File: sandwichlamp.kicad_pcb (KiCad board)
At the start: 2 copper layers, 96 x 96 mm, 7 parts, among them J1 Conn_01x01_Pin, J2 Conn_01x01_Pin, J3 Conn_01x01_Pin, U1 magnetic-charger, U2 esp32-wemos-d1-mini, U3 hw357

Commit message: Update PCB
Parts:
- added J4: 12V Enable, Connector_PinHeader_2.54mm:PinHeader_1x01_P2.54mm_Vertical, F.Cu at (79.9, 91.0)
- added SW1: SW_SPDT, Connector_PinHeader_2.54mm:PinHeader_1x03_P2.54mm_Vertical, F.Cu at (81.3, 100.1)
- moved J2 0.22 mm to (136.5, 120.8), turned to -120 degrees
- moved J1 0.20 mm to (100.0, 58.0)
- moved J3 0.16 mm to (63.6, 120.9), turned to 120 degrees
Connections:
- U2 pad 1: unconnected-(U2-GND-Pad1) -> GND
- U2 pad 16: unconnected-(U2-3V3-Pad16) -> +3V3
- U2 pad 22: unconnected-(U2-GND-Pad22) -> GND
- U2 pad 33: unconnected-(U2-GND-Pad33) -> GND
- U2 pad 35: unconnected-(U2-VCC_(USB)-Pad35) -> +5V
- U3 pad 2: unconnected-(U3-IN--Pad2) -> GND
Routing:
- added copper zone on B.Cu, net GND

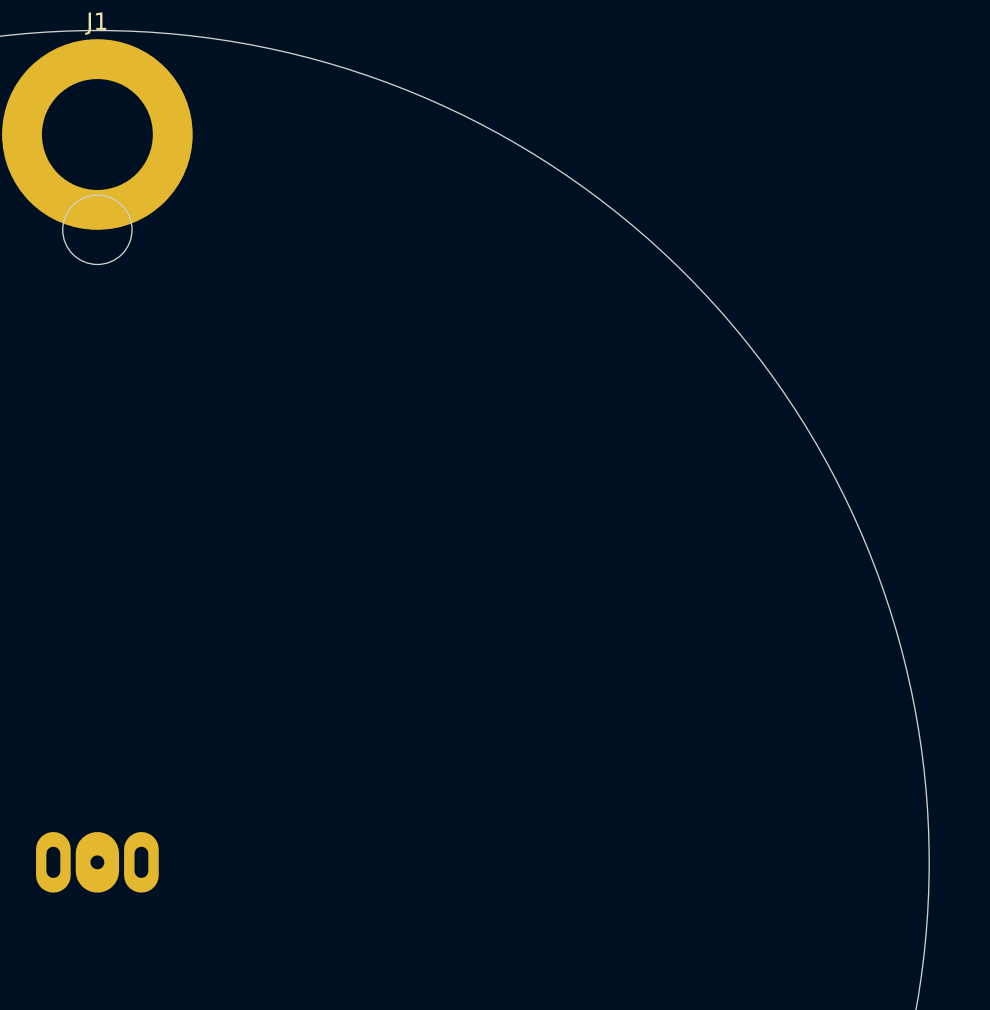
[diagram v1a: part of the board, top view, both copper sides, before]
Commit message: Add radar sensor
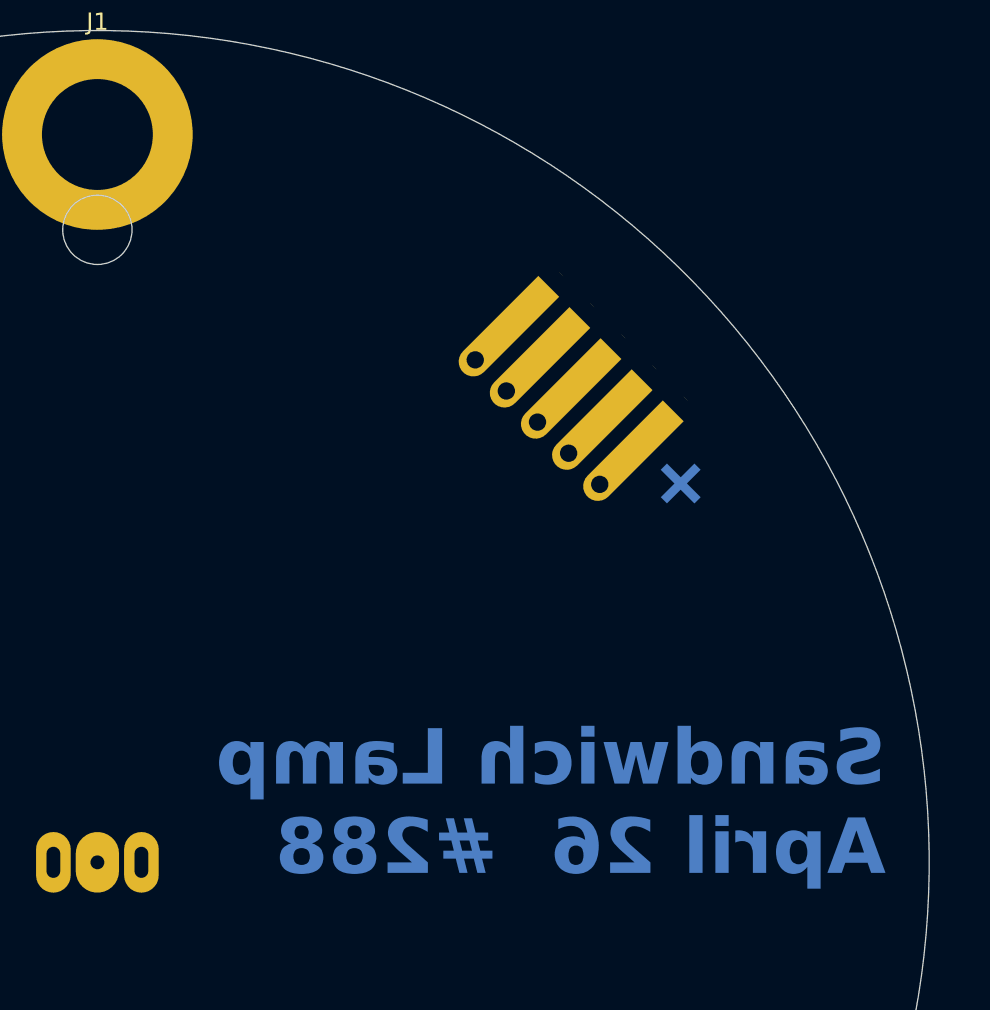
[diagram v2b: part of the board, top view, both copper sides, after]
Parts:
- added J8: HLK-LD2410C, Connector_PinHeader_2.54mm:PinHeader_1x05_P2.54mm_Vertical, B.Cu at (129.0, 78.2)
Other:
- board text added: "Sandwich Lamp April 26 #288"

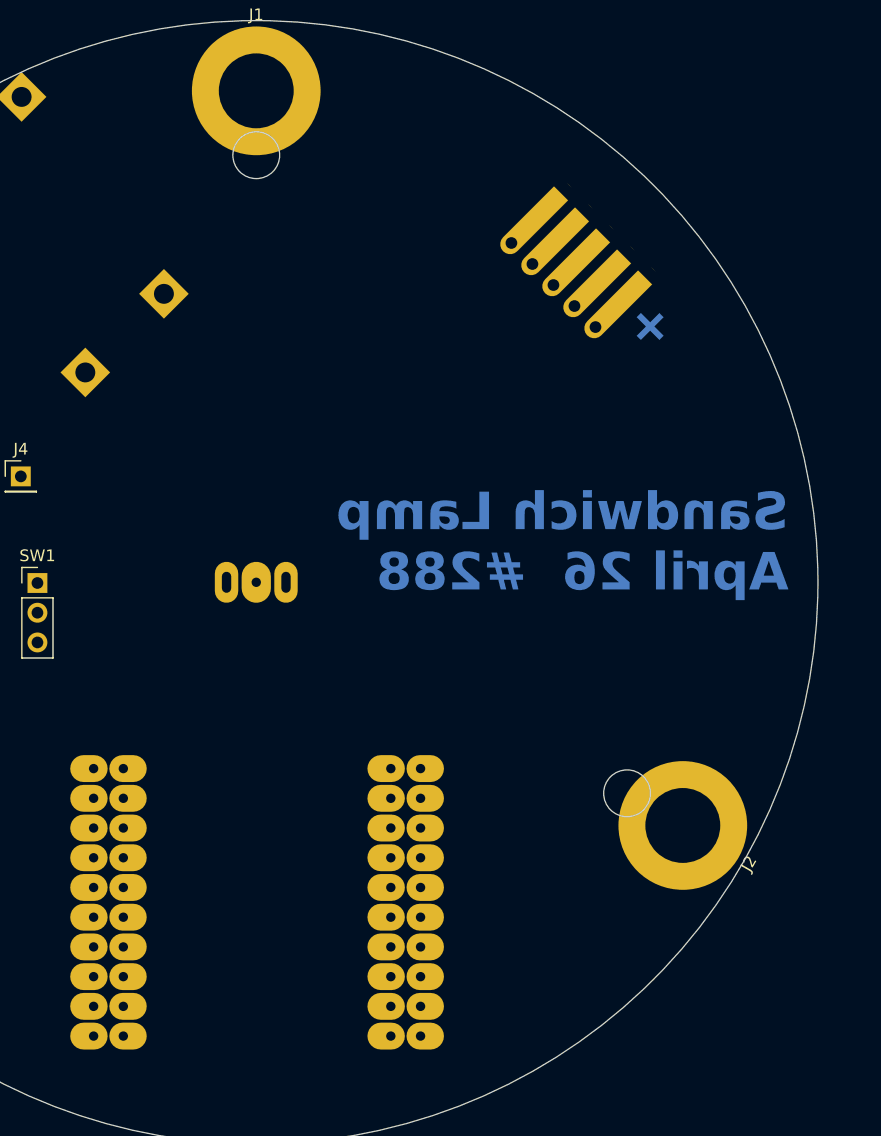
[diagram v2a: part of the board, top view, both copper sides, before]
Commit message: Align the radar with the cable
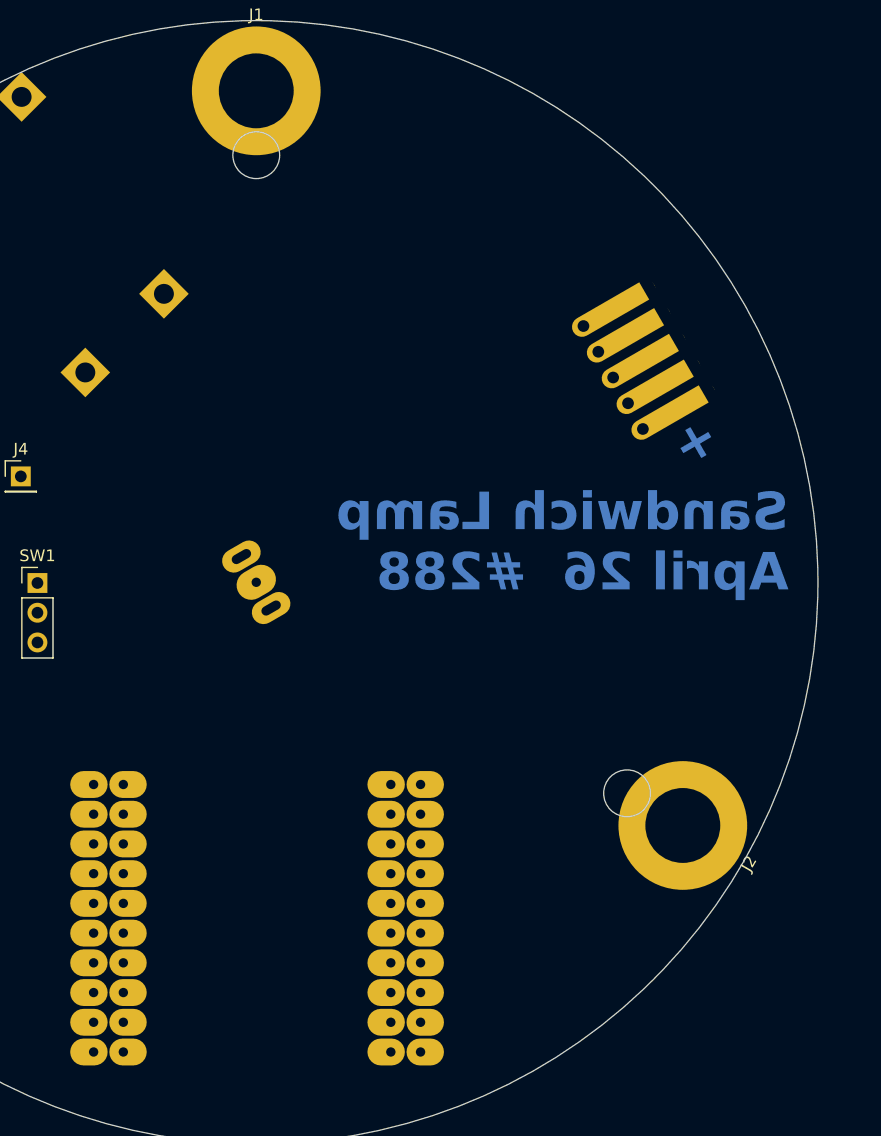
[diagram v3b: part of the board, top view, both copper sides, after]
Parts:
- moved J8 9.61 mm to (133.0, 86.9), turned to 30 degrees
- moved U2 1.36 mm to (100.1, 128.7)
- turned U1 to 120 degrees
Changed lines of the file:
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@@
 	(footprint "Connector_PinHeader_2.54mm:PinHeader_1x05_P2.54mm_Vertical"
 		(layer "B.Cu")
-		(at 128.988567 78.188567 45)
+		(at 133.04 86.899409 30)
 		(descr "Through hole straight pin header, 1x05, 2.54mm pitch, single row")
 		(tags "Through hole pin header THT 1x05 2.54mm single row")
 		(property "Reference" "J8"
-			(at 0 2.33 -135)
+			(at 0 2.33 30)
 			(layer "B.SilkS")
 			(effects
@@
 		)
 		(property "Value" "HLK-LD2410C"
-			(at 0 -12.49 -135)
+			(at 0 -12.490001 30)
 			(layer "B.Fab")
 			(effects
@@
 		)
 		(property "Footprint" ""
-			(at 0 0 -135)
+			(at 0 0 30)
 			(layer "F.Fab")
 			(hide yes)
@@
 		)
 		(property "Datasheet" ""
-			(at 0 0 -135)
+			(at 0 0 30)
 			(layer "F.Fab")
 			(hide yes)
@@
 		)
 		(property "Description" "Generic connector, single row, 01x05, script generated (kicad-library-utils/schlib/autogen/connector/)"
-			(at 0 0 -135)
+			(at 0 0 30)
 			(layer "F.Fab")
 			(hide yes)
@@
 		)
 		(property "Price" "4"
-			(at 189.916309 -70.530043 -45)
+			(at 189.91631 -70.530043 120)
 			(layer "B.Fab")
 			(hide yes)
@@
 		)
 		(property "URL" "https://de.aliexpress.com/item/1005005400130647.html"
-			(at 189.916309 -70.530043 -45)
+			(at 189.91631 -70.530043 120)
 			(layer "B.Fab")
 			(hide yes)
@@
 		)
 		(fp_line
-			(start -1.8 -11.95)
-			(end 1.8 -11.95)
+			(start -1.799999 -11.95)
+			(end 1.799999 -11.95)
 			(stroke
 				(width 0.05)
@@
 		)
 		(fp_line
-			(start 1.8 -11.95)
-			(end 1.8 1.8)
+			(start 1.799999 -11.95)
+			(end 1.799999 1.8)
 			(stroke
 				(width 0.05)
@@
 		)
 		(fp_line
-			(start -1.8 1.8)
-			(end -1.8 -11.95)
+			(start -1.8 1.799999)
+			(end -1.799999 -11.95)
 			(stroke
 				(width 0.05)
@@
 		)
 		(fp_line
-			(start 1.8 1.8)
-			(end -1.8 1.8)
+			(start 1.799999 1.8)
+			(end -1.8 1.799999)
 			(stroke
 				(width 0.05)
@@
 		)
 		(fp_text user "+"
-			(at 1.5 1.5 -135)
+			(at 1.5 1.5 -150)
 			(unlocked yes)
 			(layer "B.Cu" knockout)
@@
 		)
 		(fp_text user "${REFERENCE}"
-			(at 0 -5.079999 -45)
+			(at 0 -5.08 120)
 			(layer "B.Fab")
 			(effects
@@
 		)
 		(pad "" np_thru_hole circle
-			(at 6.5 -5 45)
+			(at 6.5 -5 30)
 			(size 0.8 0.8)
 			(drill oval 1 22)
@@
 		)
 		(pad "" np_thru_hole circle
-			(at 8.25 8.500001 90)
+			(at 8.25 8.5 75)
 			(size 0.8 0.8)
 			(drill oval 1 6)
@@
 		)
 		(pad "" np_thru_hole circle
-			(at 8.4 -18.4)
+			(at 8.4 -18.400001 345)
 			(size 0.8 0.8)
 			(drill oval 1 6)
@@
 		)
 		(pad "1" thru_hole oval
-			(at 0 0 45)
+			(at 0 0 30)
 			(size 8 1.7)
 			(drill 1
@@
 		)
 		(pad "2" thru_hole oval
-			(at 0 -2.54 45)
+			(at 0 -2.54 30)
 			(size 8 1.7)
 			(drill 1
@@
 		)
 		(pad "3" thru_hole oval
-			(at 0 -5.079999 45)
+			(at 0 -5.08 30)
 			(size 8 1.7)
 			(drill 1
@@
 		)
 		(pad "4" thru_hole oval
-			(at 0 -7.62 45)
+			(at 0 -7.62 30)
 			(size 8 1.7)
 			(drill 1
@@
 		)
 		(pad "5" thru_hole oval
-			(at 0 -10.16 45)
+			(at 0 -10.16 30)
 			(size 8 1.7)
 			(drill 1
@@
 	(footprint "magnetic-charger:magnetic-charger"
 		(layer "B.Cu")
-		(at 100 100 180)
+		(at 100 100 120)
 		(property "Reference" "U1"
-			(at 0 2.54 0)
+			(at 0 2.54 -60)
 			(unlocked yes)
 			(layer "B.SilkS")
@@
 		)
 		(property "Value" "magnetic-charger"
-			(at 10.16 14.2 0)
+			(at 10.16 14.2 -60)
 			(unlocked yes)
 			(layer "B.Fab")
@@
 		)
 		(property "Footprint" "magnetic-charger:magnetic-charger"
-			(at 0 0 0)
+			(at 0 0 120)
 			(layer "B.Fab")
 			(hide yes)
@@
 		)
 		(property "Datasheet" ""
-			(at 0 0 0)
+			(at 0 0 120)
 			(layer "B.Fab")
 			(hide yes)
@@
 		)
 		(property "Description" ""
-			(at 0 0 0)
+			(at 0 0 120)
 			(layer "B.Fab")
 			(hide yes)
@@
 		(sheetfile "sandwichlamp.kicad_sch")
 		(attr through_hole)
+		(fp_line
+			(start 0.5 -14)
+			(end 0.5 -8)
+			(stroke
+				(width 0.1)
+				(type dot)
+			)
+			(layer "B.SilkS")
+		)
+		(fp_line
+			(start -0.5 -13.5)
+			(end 0.5 -14)
+			(stroke
+				(width 0.1)
+				(type dot)
+			)
+			(layer "B.SilkS")
+		)
+		(fp_line
+			(start 1.5 -8)
+			(end 1.5 -6)
+			(stroke
+				(width 0.1)
+				(type dot)
+			)
+			(layer "B.SilkS")
+		)
+		(fp_line
+			(start -0.5 -8)
+			(end -0.5 -13.5)
+			(stroke
+				(width 0.1)
+				(type dot)
+			)
+			(layer "B.SilkS")
+		)
+		(fp_line
+			(start -1.5 -8)
+			(end 1.5 -8)
+			(stroke
+				(width 0.1)
+				(type dot)
+			)
+			(layer "B.SilkS")
+		)
+		(fp_line
+			(start -1.5 -6)
+			(end -1.5 -8)
+			(stroke
+				(width 0.1)
+				(type dot)
+			)
+			(layer "B.SilkS")
+		)
 		(fp_circle
 			(center 0 0)
@@
 			(stroke
 				(width 0.12)
-				(type solid)
+				(type dot)
 			)
 			(fill none)
@@
 		)
 		(fp_text user "${REFERENCE}"
-			(at 10.16 12.7 0)
+			(at 10.16 12.7 -60)
 			(unlocked yes)
 			(layer "B.Fab")
@@
 		)
 		(pad "1" thru_hole oval
-			(at -2.54 0 90)
+			(at -2.54 0 30)
 			(size 3.5 2)
 			(drill oval 1.8 0.8)
@@
 		)
 		(pad "1" thru_hole oval
-			(at 2.54 0 90)
+			(at 2.54 0 30)
 			(size 3.5 2)
 			(drill oval 1.8 0.8)
@@
 		)
 		(pad "2" thru_hole oval
-			(at 0 0 180)
+			(at 0 0 120)
 			(size 2.5 3.5)
 			(drill 0.8)
@@
 	(footprint "esp32-wemos-d1-mini:esp32-wemos-d1-mini"
 		(layer "B.Cu")
-		(at 100.07 127.35 180)
+		(at 100.07 128.71 180)
 		(property "Reference" "U2"
 			(at -3.81 -1.27 0)
@@
 			)
 		)
+	)
+	(gr_line
+		(start 100 100)
+		(end 141.568668 76.000319)
+		(stroke
+			(width 0.1)
+			(type default)
+		)
+		(layer "Dwgs.User")
 	)
 	(gr_circle
@@
 	(gr_line
 		(start 100 100)
-		(end 148.26 51.74)
+		(end 141.568668 123.999681)
 		(stroke
 			(width 0.1)
+			(type default)
+		)
+		(layer "Dwgs.User")
+	)
+	(gr_line
+		(start 100 100)
+		(end 58.430781 124)
+		(stroke
+			(width 0.1)

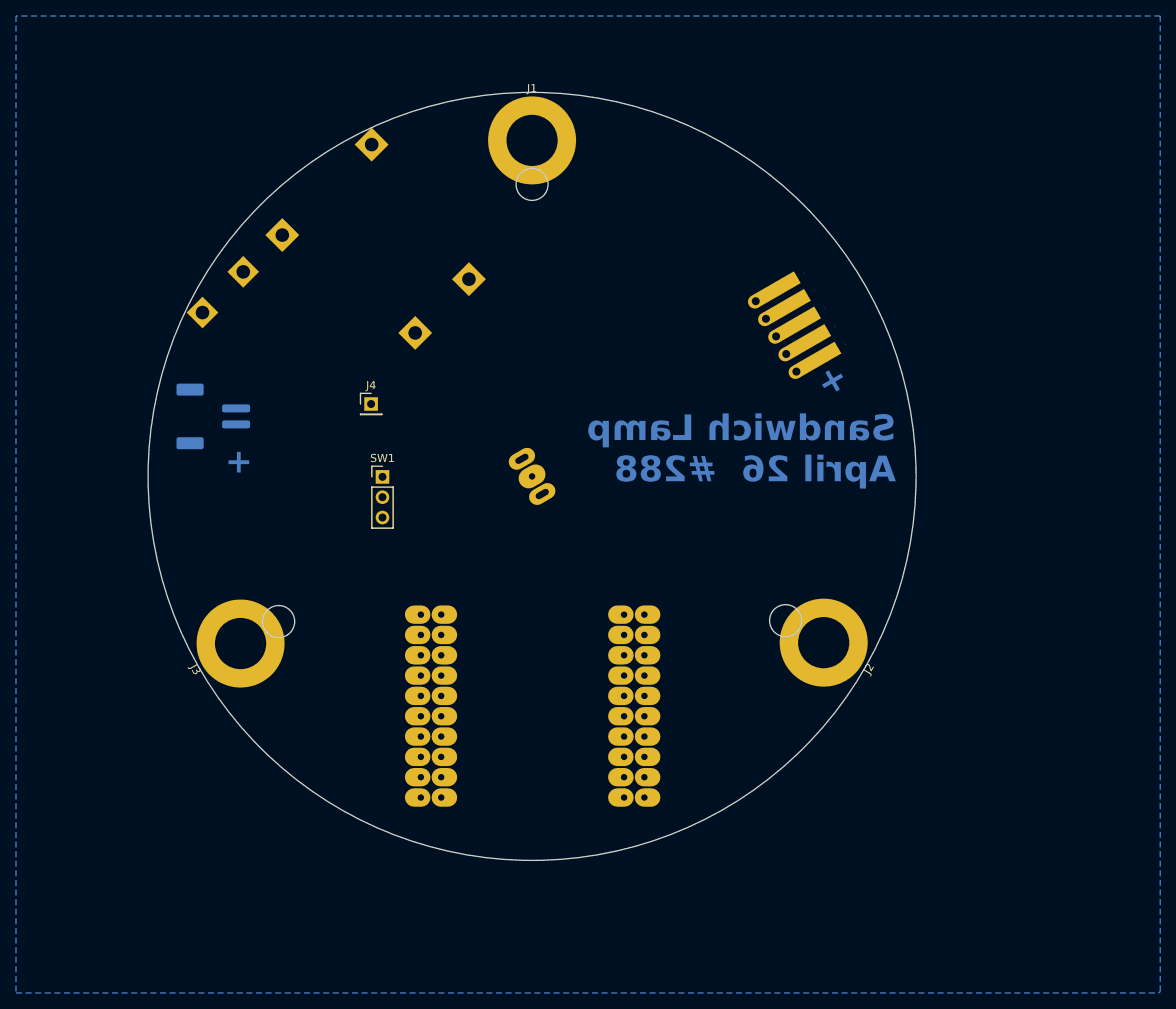
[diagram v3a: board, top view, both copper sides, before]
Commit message: Add BME280 and radio-receiver and continue with the placement of the components
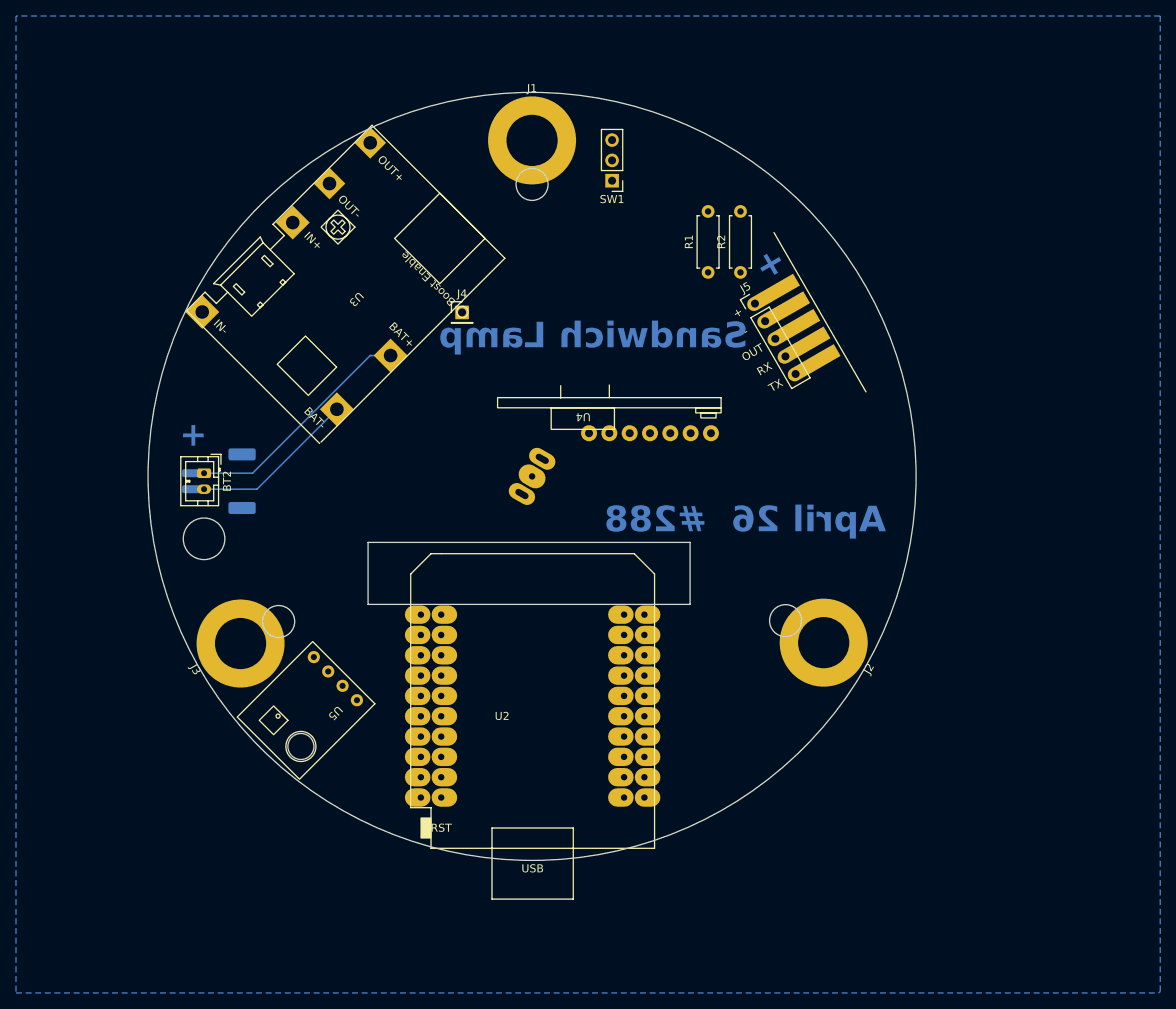
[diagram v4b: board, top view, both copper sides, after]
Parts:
- added BT2: Battery_Cell, Connector_JST:JST_PH_B2B-PH-K_1x02_P2.00mm_Vertical, F.Cu at (59.0, 99.6)
- added R1: 2k7, Resistor_THT:R_Axial_DIN0207_L6.3mm_D2.5mm_P7.62mm_Horizontal, F.Cu at (122.0, 74.5)
- added R2: 4k7, Resistor_THT:R_Axial_DIN0207_L6.3mm_D2.5mm_P7.62mm_Horizontal, F.Cu at (126.0, 74.5)
- added U4: RX480E, radio-receiver:radio-receiver, F.Cu at (122.4, 94.6)
- added U5: bme280, bme280:bme280, F.Cu at (75.4, 125.3)
- J5: renamed from J8; moved to F.Cu
- U2, U3: moved to F.Cu
- moved SW1 46.8 mm to (110.0, 63.0), turned to 180 degrees
- moved U3 33.2 mm to (96.6, 72.7), turned to -135 degrees
- moved J4 16.1 mm to (91.2, 79.5)
- moved J5 9.95 mm to (127.9, 78.4)
- moved BT1 8.13 mm to (60.9, 100.6), turned to -90 degrees
- turned U1 to -120 degrees
- turned U2 to 0 degrees
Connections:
- J5 pad 1: (no net) -> +5V
- J5 pad 2: (no net) -> GND
- J5 pad 3: (no net) -> unconnected-(J5-Pin_3-Pad3)
- J5 pad 4: (no net) -> RADAR_TX
- J5 pad 5: (no net) -> Net-(J5-Pin_5)
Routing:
- net Net-(BT1-+): track 0.00 -> 29.4 mm
- net Net-(BT1--): track 0.00 -> 20.7 mm
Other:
- outline, holes or cut-outs redrawn
- board text added: "April 26 #288"
- board text added: "Sandwich Lamp"
- board text removed: "Sandwich Lamp April 26 #288"

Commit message: Add new esp footprint
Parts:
- removed U2: esp32-wemos-d1-mini, esp32-wemos-d1-mini:esp32-wemos-d1-mini
- added J6: Conn_01x20_Pin, Connector_PinHeader_2.54mm:PinHeader_1x20_P2.54mm_Vertical, F.Cu at (124.6, 115.5)
- added J6: Conn_01x20_Pin, Connector_PinHeader_2.54mm:PinHeader_1x20_P2.54mm_Vertical, F.Cu at (76.4, 138.5)
- added U6: DS18B20, Package_TO_SOT_THT:TO-92L_Inline_Wide, F.Cu at (127.8, 125.2)
- turned U1 to 120 degrees
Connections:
- net Net-(BT1-+) renamed +4V
- BT1 pad 2: Net-(BT1--) -> GND
- BT2 pad 2: Net-(BT1--) -> GND
- SW1 pad 2: unconnected-(SW1-B-Pad2) -> VBUS
- SW1 pad 3: unconnected-(SW1-C-Pad3) -> Net-(D2-K)
- U3 pad 1: unconnected-(U3-IN+-Pad1) -> VBUS
- U3 pad 3: unconnected-(U3-O+-Pad3) -> +12V
- U3 pad 4: unconnected-(U3-O--Pad4) -> GND
- U3 pad 6: Net-(BT1--) -> GND
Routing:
- net Net-(BT1--): track 20.7 -> 0.00 mm
- net GND: track 0.00 -> 20.7 mm
